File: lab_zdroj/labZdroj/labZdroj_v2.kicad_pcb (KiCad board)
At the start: 2 copper layers, 40 parts, among them J1 24V st, J2 0-30V ss, T1 BC327, T2 BC547, T3 BC547, U1 LM350_TO220

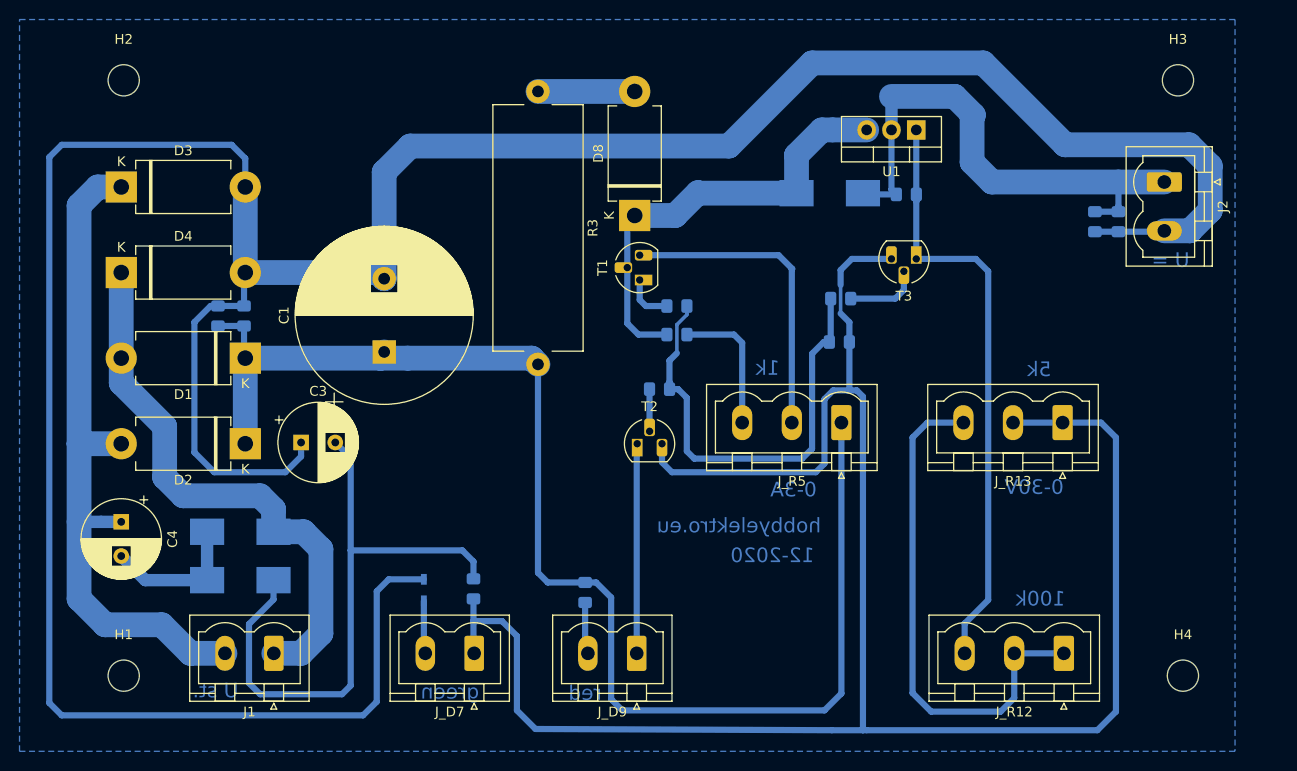
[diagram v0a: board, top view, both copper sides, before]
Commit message: final pcb, předěláno na tranzistory v tht provedení.
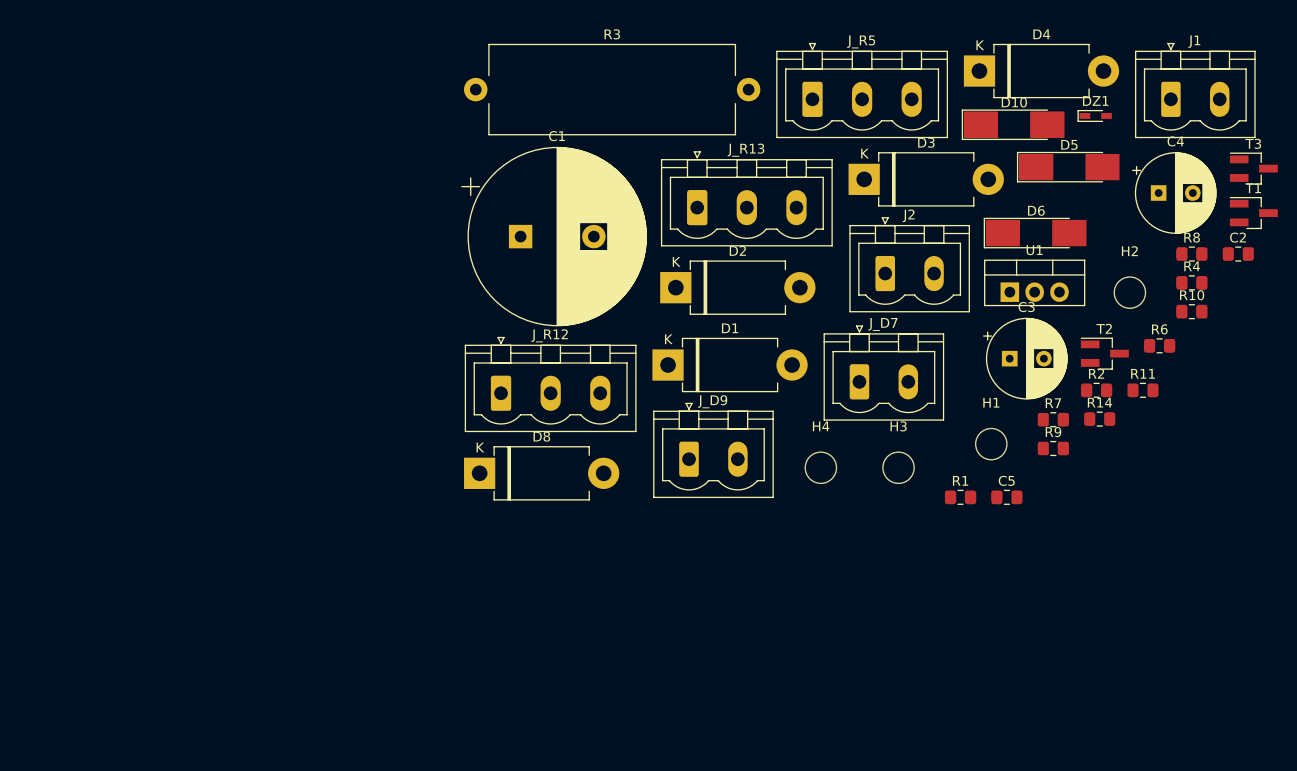
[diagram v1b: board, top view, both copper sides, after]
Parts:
- C2, C5, D10, D5, D6, DZ1, R1, R10, R11, R14, R2, R4, R6, R7, R8, R9: moved to F.Cu
- T1, T2, T3: footprint Package_TO_SOT_THT:TO-92L_HandSolder -> Package_TO_SOT_SMD:SOT-23_Handsoldering
- moved C4 111.4 mm to (156.0, 77.5), turned to 0 degrees
- moved J1 108.0 mm to (157.3, 67.9), turned to 0 degrees
- moved H2 105.3 mm to (153.1, 87.7)
- moved C2 104.7 mm to (164.2, 83.7), turned to 0 degrees
- moved D5 92.7 mm to (146.9, 74.8), turned to 0 degrees
- moved H1 91.9 mm to (138.9, 103.2)
- moved D4 90.3 mm to (137.7, 65.0)
- moved D6 88.9 mm to (143.5, 81.6)
- moved DZ1 84.2 mm to (149.6, 69.6), turned to 0 degrees
- moved D3 76.1 mm to (125.9, 76.1)
- moved R1 75.7 mm to (135.7, 108.6), turned to 0 degrees
- moved C3 73.1 mm to (140.8, 94.4)
- moved R2 67.0 mm to (149.7, 97.7), turned to 0 degrees
- moved J_R12 63.5 mm to (88.7, 98.0), turned to 0 degrees
- moved T1 63.3 mm to (165.8, 79.5), turned to 0 degrees
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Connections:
- J2 pad 1: Net-(C5-Pad1) -> GND
- J2 pad 2: GND -> Net-(C5-Pad1)
- J_D7 pad 1: Net-(J_D7-Pad1) -> Net-(DZ1-Pad2)
- J_D7 pad 2: Net-(DZ1-Pad2) -> Net-(J_D7-Pad2)
- J_R12 pad 2: Net-(J_R12-Pad1) -> Net-(J_R12-Pad2)
- J_R12 pad 3: Net-(J_R12-Pad3) -> Net-(J_R12-Pad2)
- J_R13 pad 1: Net-(J_D7-Pad1) -> Net-(J_R12-Pad2)
- J_R13 pad 2: Net-(J_D7-Pad1) -> Net-(J_D7-Pad2)
- J_R13 pad 3: Net-(J_R12-Pad1) -> Net-(J_D7-Pad2)
- J_R5 pad 1: +24V -> Net-(J_R5-Pad1)
- J_R5 pad 3: Net-(J_R5-Pad3) -> +24V
- R11 pad 2: Net-(J_R12-Pad3) -> Net-(J_R12-Pad1)
- R2 pad 1: Net-(J_D7-Pad1) -> Net-(J_D7-Pad2)
- R4 pad 2: Net-(J_R5-Pad3) -> Net-(J_R5-Pad1)
- R7 pad 2: Net-(J_D7-Pad1) -> Net-(J_D7-Pad2)
- T2 pad 3: Net-(J_D7-Pad1) -> Net-(J_D7-Pad2)
- T3 pad 1: Net-(J_R12-Pad3) -> Net-(J_R12-Pad1)
- T3 pad 3: Net-(J_D7-Pad1) -> Net-(J_D7-Pad2)
- U1 pad 1: Net-(J_R12-Pad3) -> Net-(J_R12-Pad1)
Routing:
- net GND: track 312.7 -> 0.00 mm
- net Net-(J_D7-Pad1): track 203.6 -> 0.00 mm
- net +24V: track 138.6 -> 0.00 mm
- net Net-(C4-Pad1): track 71.3 -> 0.00 mm
- net Net-(C3-Pad2): track 63.2 -> 0.00 mm
- net Net-(J_R12-Pad3): track 61.2 -> 0.00 mm
- net Net-(D1-Pad2): track 57.5 -> 0.00 mm
- net Net-(C5-Pad1): track 53.7 -> 0.00 mm
- net Net-(J_R12-Pad1): track 53.4 -> 0.00 mm
- net Net-(R10-Pad2): track 46.9 -> 0.00 mm
- net Net-(D10-Pad1): track 45.6 -> 0.00 mm
- net Net-(J_R5-Pad2): track 32.0 -> 0.00 mm
- net Net-(J_D9-Pad1): track 21.5 -> 0.00 mm
- net Net-(C4-Pad2): track 14.8 -> 0.00 mm
- net Net-(J_R5-Pad3): track 14.2 -> 0.00 mm
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- removed copper zone on B.Cu, net GND
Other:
- board text removed: "0-30V"
- board text removed: "0-3A"
- board text removed: "100k"
- board text removed: "12-2020"
- board text removed: "1k"
- board text removed: "5k"
- board text removed: "U ="
- board text removed: "U st."
- board text removed: "green"
- board text removed: "hobbyelektro.eu"
- board text removed: "red"
